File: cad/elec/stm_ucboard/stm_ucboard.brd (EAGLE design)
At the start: 34 x 14 mm, 21 parts

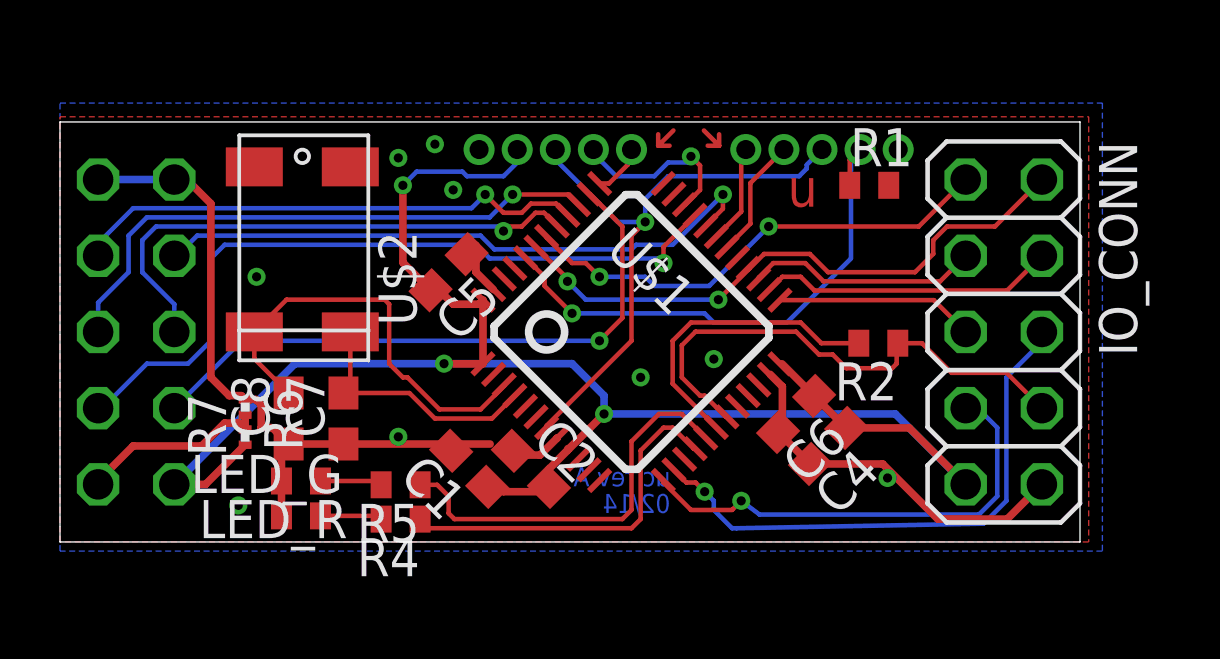
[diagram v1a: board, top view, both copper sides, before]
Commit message: added pullup/pulldown resistors to the rf pins ; connected PA0 (WKUP1) to external IO interface
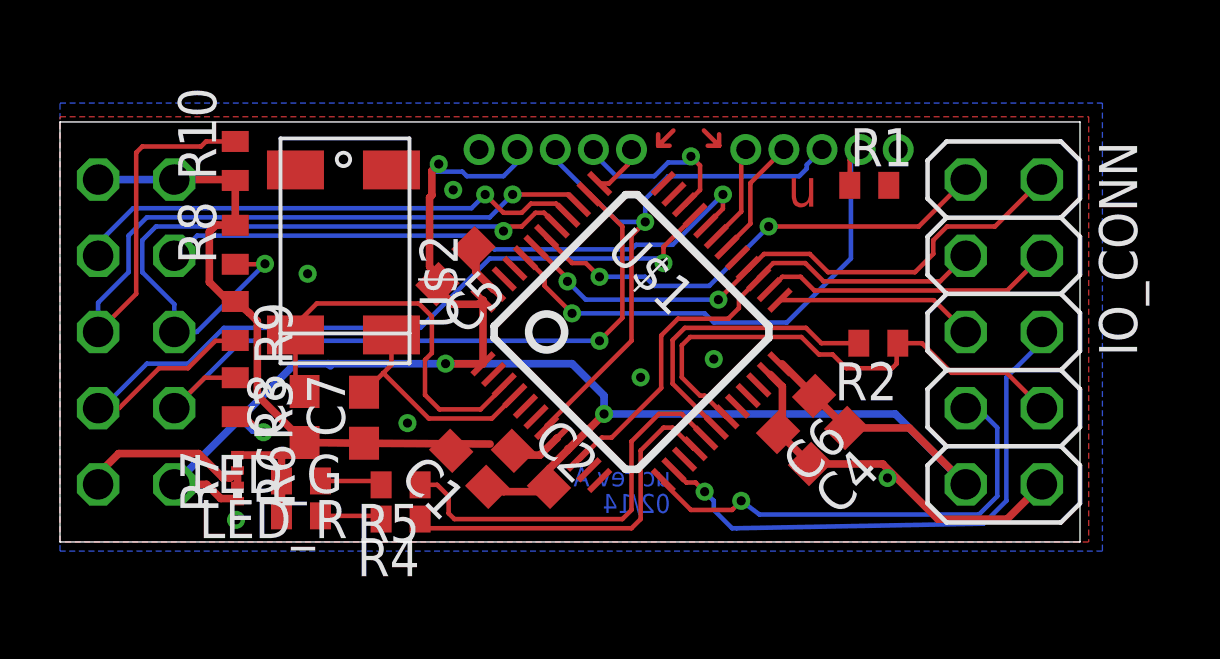
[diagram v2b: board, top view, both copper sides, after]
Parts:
- added R10, R3, R8, R9: 1M, rcl:R0402
- moved R7 1.90 mm to (5.92, 1.62)
- moved R6 1.87 mm to (5.92, 2.64)
- moved U$2 1.38 mm to (9.45, 9.65)
- moved C7 0.69 mm to (10.1, 4.14)
- moved C8 0.54 mm to (8.15, 4.17)
- moved C5 0.31 mm to (13.2, 9.19)
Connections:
- net +3V3: now also R3.2
- net GND: now also R10.1, R8.2, R9.1
- net IO_2: now also U$1.10
- net RF_CE: now also R9.2
- net RF_CSN: now also R3.1
- net RF_MO: now also R8.1
- net RF_SCK: now also R10.2
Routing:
- net RF_SCK: track 19.3 -> 29.3 mm
- net IO_2: track 7.75 -> 17.5 mm
- net RF_MO: track 18.0 -> 23.0 mm, vias 1 -> 2
- net RF_CE: track 25.0 -> 28.5 mm
- net GND: track 39.6 -> 42.4 mm, vias 9 -> 7
- net RF_CSN: track 20.8 -> 23.2 mm
- net +3V3: track 60.2 -> 61.2 mm, vias 3 -> 4
- net N$5: track 8.51 -> 7.62 mm
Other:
- board text added: "IO"
- board text added: "RF"
